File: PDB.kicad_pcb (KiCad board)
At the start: 2 copper layers, 50 x 80 mm, 87 parts, among them J1 Conn_01x02, J10 Conn_01x02_MountingPin, J11 USB_C_Receptacle_USB2.0, J2 Conn_01x02, J3 Conn_01x02, J4 Conn_01x02, J5 Conn_01x02, J6 Conn_01x02, J7 Conn_01x02, J8 Conn_01x02, J9 Conn_02x03_Odd_Even, SW1 SW_Push, U1 ATmega2560-16AU, U2 LMZM23600, U3 LMZ13608, U4 LTC2946, U5 LTC2946, U6 FT230XQ, Y1 16MHz

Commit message: more layout
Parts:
- moved R11 124.5 mm to (95.5, 122.0)
- moved SW1 85.4 mm to (110.0, 69.2)
- moved R15 73.6 mm to (91.5, 111.2)
- moved R14 73.5 mm to (91.5, 108.0)
- moved R13 45.1 mm to (107.5, 123.5)
- moved R12 44.9 mm to (107.5, 121.8)
- moved R2 10.9 mm to (88.0, 108.0), turned to 90 degrees
- moved R1 9.65 mm to (89.8, 108.0), turned to 90 degrees
- moved C4 1.00 mm to (97.8, 102.2)
- moved C7 0.50 mm to (98.8, 122.0)
- moved Y1 0.50 mm to (100.8, 125.0)
- moved R16 0.25 mm to (98.5, 95.0)
- moved R17 0.25 mm to (96.8, 95.0)
- moved R18 0.25 mm to (84.2, 83.5)
- moved R19 0.25 mm to (87.2, 83.5)
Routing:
- net +3V3: track 14.3 -> 155.6 mm, vias 0 -> 7
- net /ATMega/~RESET~: track 0.00 -> 133.5 mm, vias 0 -> 4
- net /SCL: track 0.00 -> 82.0 mm, vias 0 -> 3
- net /SDA: track 0.00 -> 81.9 mm, vias 0 -> 3
- net /~ALERT_VBAT~: track 0.00 -> 61.8 mm, vias 0 -> 2
- net /ATMega/MISO: track 0.00 -> 61.2 mm, vias 0 -> 1
- net /ATMega/SCK: track 0.00 -> 55.5 mm, vias 0 -> 1
- net /~ALERT_+5V~: track 0.00 -> 54.5 mm, vias 0 -> 2
- net /ATMega/MOSI: track 0.00 -> 53.4 mm, vias 0 -> 1
- net +BATT: track 49.3 -> 99.6 mm, vias 5 -> 7
- net /TX: track 4.08 -> 26.1 mm, vias 0 -> 2
- net Net-(C17-Pad1): track 10.0 -> 16.1 mm, vias 2 -> 3
- net /RX: track 19.0 -> 21.3 mm
- net Net-(C18-Pad1): track 0.00 -> 1.87 mm
- net VBUS: track 13.5 -> 14.1 mm
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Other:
- net class Default: via_dia 0.8 -> 0.5; via_drill 0.4 -> 0.25
- rule trace_min: 0.1 -> 0.15
- board text removed: "Todo: Not use min size Vias Adhere to design rules + safety margin"

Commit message: even more layout
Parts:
- added D11: LED, LED_SMD:LED_0603_1608Metric, F.Cu at (68.0, 102.5)
- added D12: LED, LED_SMD:LED_0603_1608Metric, F.Cu at (68.0, 104.2)
- added D13: LED, LED_SMD:LED_0603_1608Metric, F.Cu at (68.0, 106.0)
- added JP1: Jumper, Connector_PinHeader_2.54mm:PinHeader_1x02_P2.54mm_Vertical, F.Cu at (71.0, 122.5)
- added JP2: Jumper, Connector_PinHeader_2.54mm:PinHeader_1x02_P2.54mm_Vertical, F.Cu at (71.0, 118.8)
- added R28: 470, Resistor_SMD:R_0603_1608Metric, F.Cu at (71.2, 102.5)
- added R29: 470, Resistor_SMD:R_0603_1608Metric, F.Cu at (71.2, 104.2)
- added R30: 270, Resistor_SMD:R_0603_1608Metric, F.Cu at (71.2, 106.0)
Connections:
- net Net-(C13-Pad1) renamed /5V/5VIN
- C17 pad 1: Net-(C17-Pad1) -> +5V
- C18 pad 1: Net-(C18-Pad1) -> +5V
- U4 pad 1: +BATT -> +5V
- U4 pad 14: Net-(C17-Pad1) -> +5V
- U4 pad 2: Net-(C17-Pad1) -> +5V
- U5 pad 1: +BATT -> +5V
- U5 pad 2: Net-(C18-Pad1) -> +5V
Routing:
- net +5V: track 35.2 -> 102.5 mm, vias 0 -> 5
- net /5V/5VIN: track 13.9 -> 57.6 mm, vias 0 -> 1
- net +BATT: track 99.6 -> 124.7 mm
- net /FT230/5VOUT: track 9.45 -> 26.1 mm, vias 0 -> 1
- net Net-(C17-Pad1): track 16.1 -> 0.00 mm, vias 3 -> 0
- net GNDS: track 8.14 -> 16.3 mm
- net +3V3: track 155.6 -> 163.7 mm, vias 7 -> 8
- net VBUS: track 14.1 -> 12.0 mm
- net Net-(C18-Pad1): track 1.87 -> 0.00 mm
- net Net-(D13-Pad2): track 0.00 -> 1.68 mm
- net Net-(D12-Pad2): track 0.00 -> 1.68 mm
- net Net-(D11-Pad2): track 0.00 -> 1.68 mm
- net Net-(D10-Pad1): track 11.5 -> 11.4 mm, vias 0 -> 2

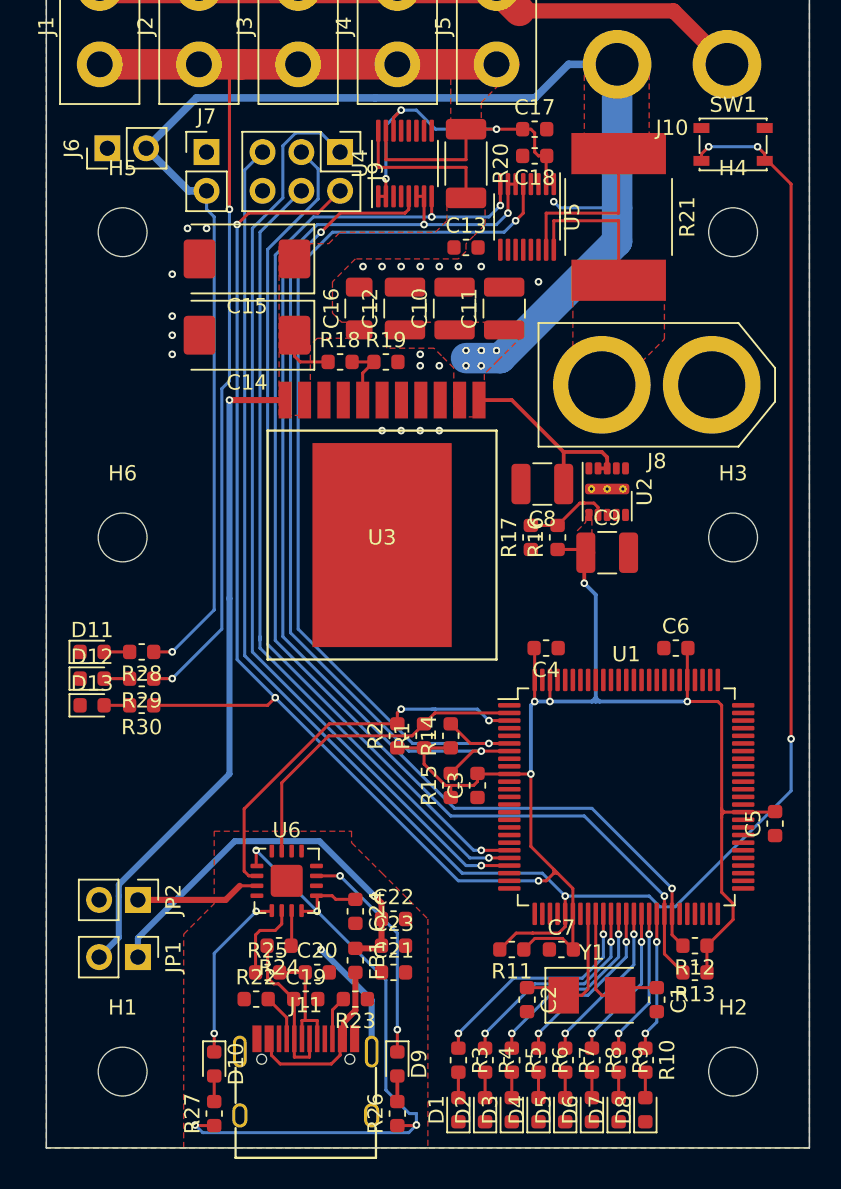
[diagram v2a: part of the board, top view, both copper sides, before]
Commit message: layout fixes, reannotate
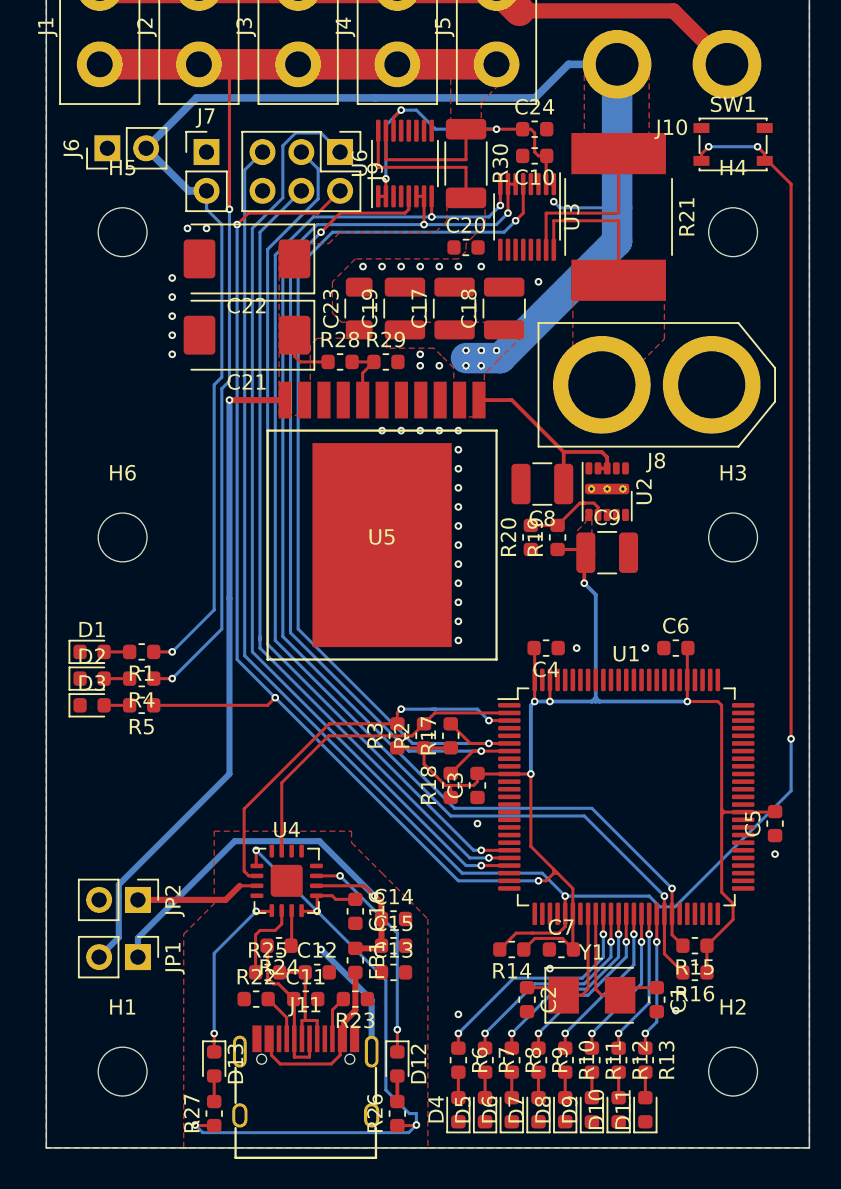
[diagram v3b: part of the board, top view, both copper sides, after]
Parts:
- renumbered C18 to C10, C19 to C11, C20 to C12, C21 to C13, C22 to C14, C23 to C15, C24 to C16, C10 to C17, C11 to C18, C12 to C19, C13 to C20, C14 to C21, C15 to C22, C16 to C23, C17 to C24, D11 to D1, D7 to D10, D8 to D11, D9 to D12, D10 to D13, D12 to D2, D13 to D3, D1 to D4, D2 to D5, D3 to D6, D4 to D7, D5 to D8, D6 to D9, R28 to R1, R7 to R10, R8 to R11, R9 to R12, R10 to R13, R11 to R14, R12 to R15, R13 to R16, R14 to R17, R15 to R18, R16 to R19, R1 to R2, R17 to R20, R18 to R28, R19 to R29, R2 to R3, R20 to R30, R29 to R4, R30 to R5, R3 to R6, R4 to R7, R5 to R8, R6 to R9, U5 to U3, U6 to U4, U3 to U5, U4 to U6
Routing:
- net /FT230/5VOUT: track 26.1 -> 30.2 mm
- net GND: vias 21 -> 41

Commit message: the ACTUAL silkscreen stuff, including the actual changes this time
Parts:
- added REF**: OSHW-Symbol_8.9x8mm_SilkScreen, Symbol:OSHW-Symbol_8.9x8mm_SilkScreen, F.Cu at (70.0, 87.2)
- added REF**: ToolboxLogo, Toolbox:ToolboxLogo, F.Cu at (82.0, 109.0)
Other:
- board text added: "REMOVE BEFORE FLIGHT"

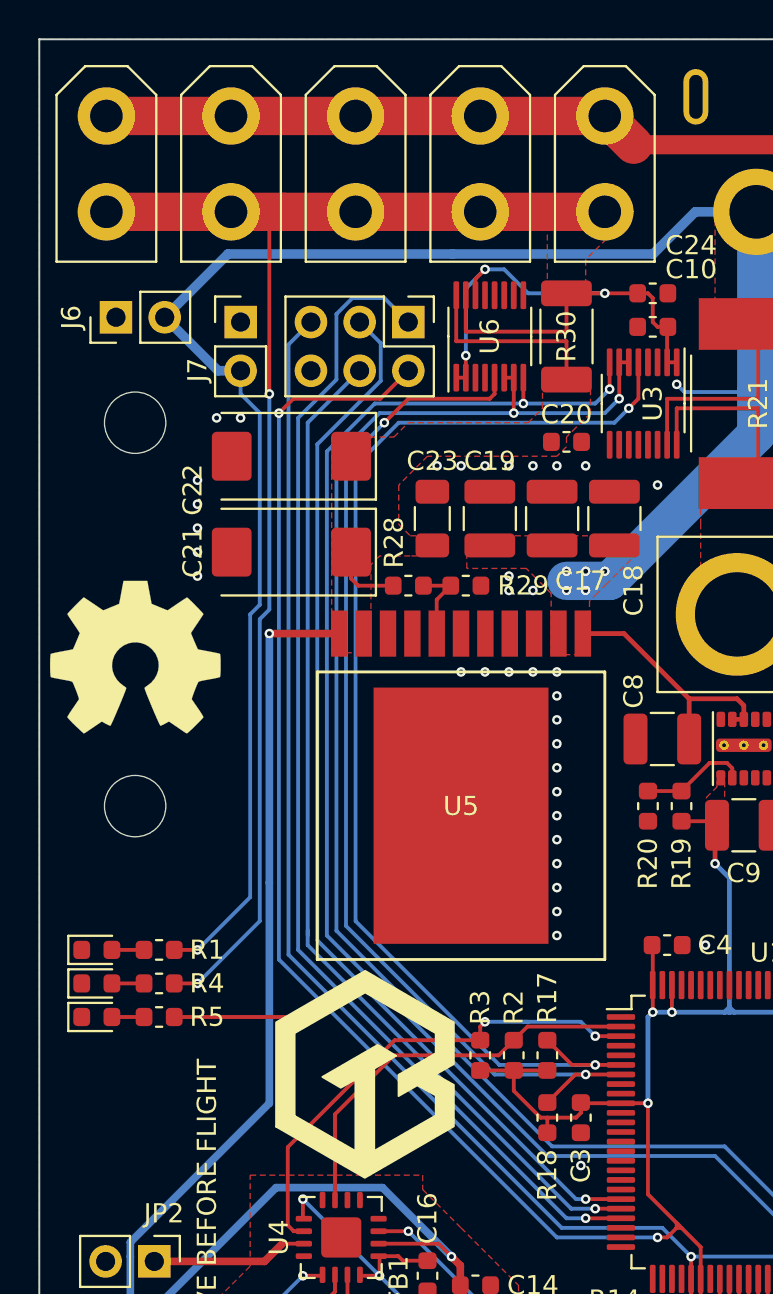
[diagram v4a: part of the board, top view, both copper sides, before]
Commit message: use official XT30 footprint
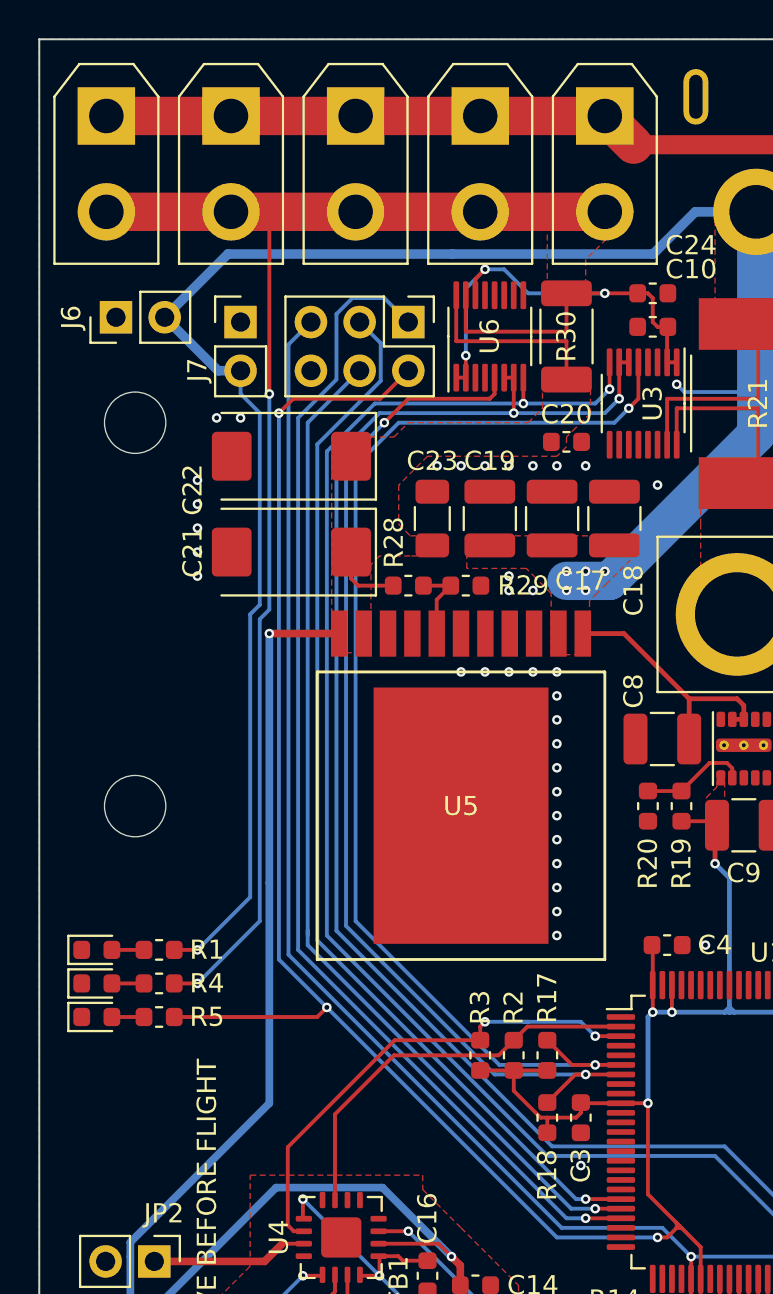
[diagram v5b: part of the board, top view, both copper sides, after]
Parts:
- removed REF**: OSHW-Symbol_8.9x8mm_SilkScreen, Symbol:OSHW-Symbol_8.9x8mm_SilkScreen
- removed REF**: ToolboxLogo, Toolbox:ToolboxLogo
- J1, J2, J3, J4, J5: footprint XT30:XT30PB-F -> Connector_AMASS:AMASS_XT30UPB-F_1x02_P5.0mm_Vertical
- moved J1 2.50 mm to (68.5, 59.0), turned to 270 degrees
- moved J2 2.50 mm to (75.0, 59.0), turned to 270 degrees
- moved J3 2.50 mm to (81.5, 59.0), turned to 270 degrees
- moved J4 2.50 mm to (88.0, 59.0), turned to 270 degrees
- moved J5 2.50 mm to (94.5, 59.0), turned to 270 degrees
